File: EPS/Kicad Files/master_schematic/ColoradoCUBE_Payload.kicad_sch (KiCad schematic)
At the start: 8 parts, among them U8 PIC18F27Q84-E/SP

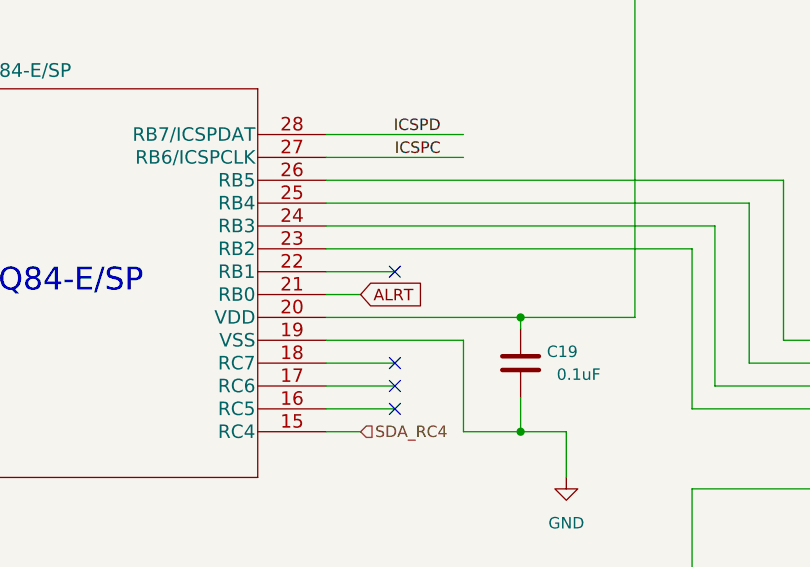
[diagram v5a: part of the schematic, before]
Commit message: EPS 2.0 update
added alert pins to microcontroller
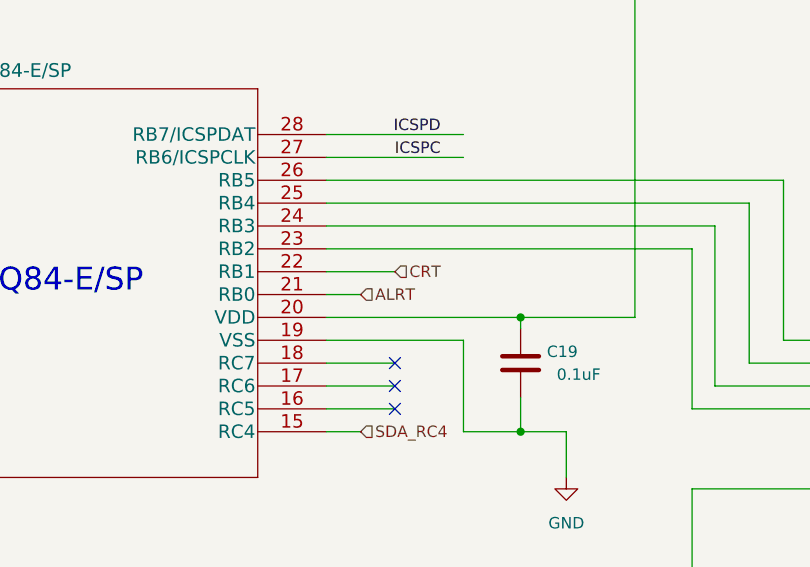
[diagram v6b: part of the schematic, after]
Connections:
- net CRT: now reaches U8.22 (RB1)
- no-connect marks 10 -> 9
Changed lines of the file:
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@@
   (no_connect (at 238.76 132.08))
   (no_connect (at 238.76 134.62))
-  (no_connect (at 238.76 119.38))
   (no_connect (at 147.32 119.38))
   (no_connect (at 147.32 124.46))
@@
     (effects (font (size 1.27 1.27)) (justify right bottom))
   )
-  (global_label "ALRT" (shape input) (at 234.95 121.92 0) (fields_autoplaced)
+  (hierarchical_label "CRT" (shape input) (at 238.76 119.38 0)
     (effects (font (size 1.27 1.27)) (justify left))
-    (property "Intersheet References" "${INTERSHEET_REFS}" (id 0) (at 241.7174 121.8406 0)
-      (effects (font (size 1.27 1.27)) (justify left) hide)
-    )
   )
   (hierarchical_label "CANH" (shape output) (at 347.98 129.54 0)
@@
     (effects (font (size 1.27 1.27)) (justify left))
   )
+  (hierarchical_label "ALRT" (shape input) (at 234.95 121.92 0)
+    (effects (font (size 1.27 1.27)) (justify left))
+  )
